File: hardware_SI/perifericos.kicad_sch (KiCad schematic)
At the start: 8 parts

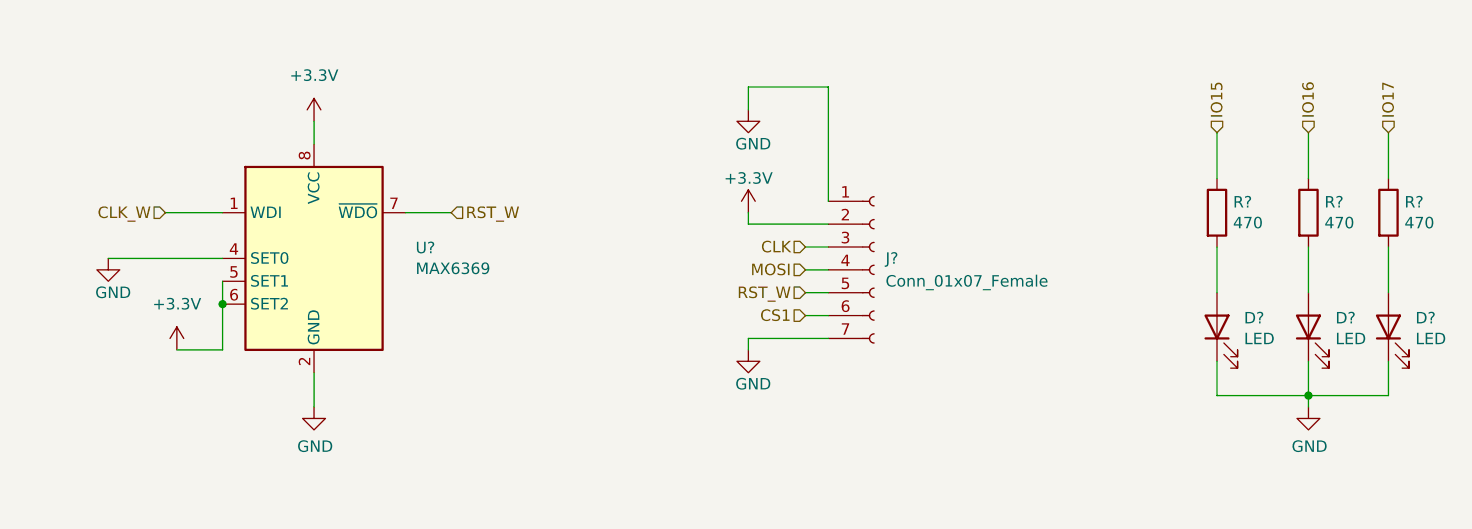
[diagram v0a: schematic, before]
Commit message: Etq compon, C desacop, ferrita
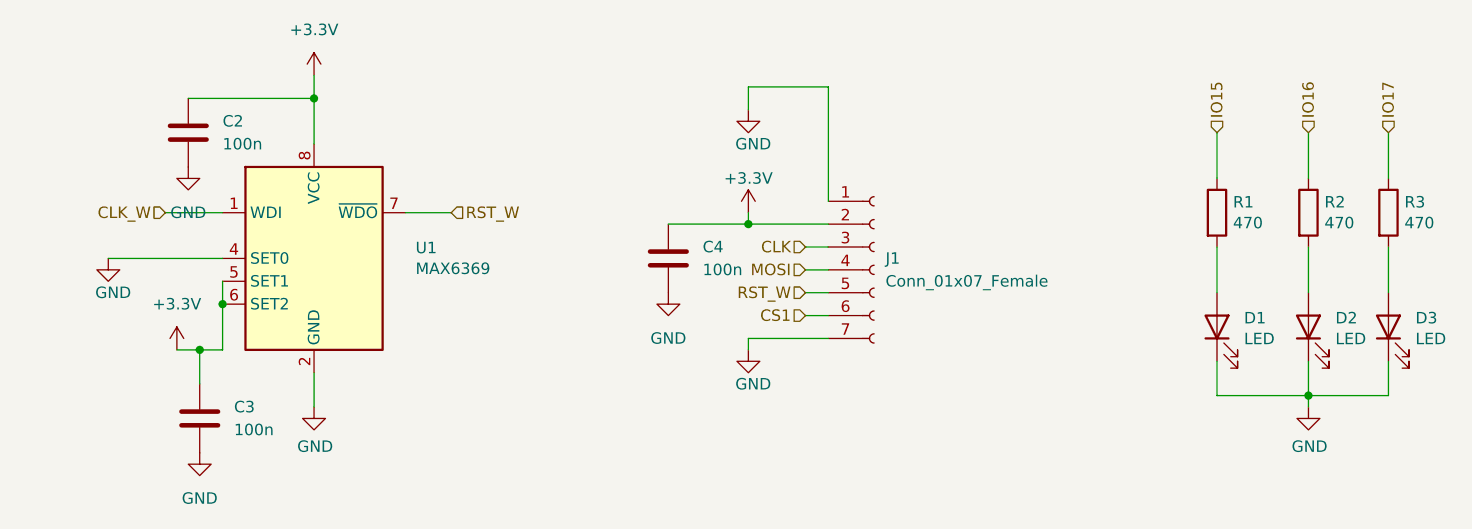
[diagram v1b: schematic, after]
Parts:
- added C2, C3, C4: 100n, symbol Device:C
- gave numbers to parts that had none: 8
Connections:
- net +3V3: now also C2.1, C3.1, C4.1
- net GND: now also C2.2, C3.2, C4.2
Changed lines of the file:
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@@
 (kicad_sch (version 20211123) (generator eeschema)
   (paper "A4")
+  (junction (at 93.98 76.2) (diameter 0) (color 0 0 0 0)
+  )
+  (junction (at 81.28 104.14) (diameter 0) (color 0 0 0 0)
+  )
   (junction (at 83.82 99.06) (diameter 0) (color 0 0 0 0)
   )
   (junction (at 204.47 109.22) (diameter 0) (color 0 0 0 0)
   )
+  (junction (at 142.24 90.17) (diameter 0) (color 0 0 0 0)
+  )
   (wire (pts (xy 151.13 90.17) (xy 142.24 90.17))
     (stroke (width 0) (type default) (color 0 0 0 0))
@@
     (stroke (width 0) (type default) (color 0 0 0 0))
   )
+  (wire (pts (xy 133.35 90.17) (xy 142.24 90.17))
+    (stroke (width 0) (type default) (color 0 0 0 0))
+  )
   (wire (pts (xy 151.13 102.87) (xy 142.24 102.87))
     (stroke (width 0) (type default) (color 0 0 0 0))
@@
     (stroke (width 0) (type default) (color 0 0 0 0))
   )
+  (wire (pts (xy 81.28 104.14) (xy 81.28 107.95))
+    (stroke (width 0) (type default) (color 0 0 0 0))
+  )
+  (wire (pts (xy 80.01 76.2) (xy 93.98 76.2))
+    (stroke (width 0) (type default) (color 0 0 0 0))
+  )
   (wire (pts (xy 213.36 85.09) (xy 213.36 80.01))
     (stroke (width 0) (type default) (color 0 0 0 0))
@@
     (stroke (width 0) (type default) (color 0 0 0 0))
   )
-  (wire (pts (xy 78.74 104.14) (xy 83.82 104.14))
+  (wire (pts (xy 78.74 104.14) (xy 81.28 104.14))
     (stroke (width 0) (type default) (color 0 0 0 0))
   )
@@
     (stroke (width 0) (type default) (color 0 0 0 0))
   )
+  (wire (pts (xy 93.98 76.2) (xy 93.98 81.28))
+    (stroke (width 0) (type default) (color 0 0 0 0))
+  )
   (wire (pts (xy 83.82 96.52) (xy 83.82 99.06))
     (stroke (width 0) (type default) (color 0 0 0 0))
@@
     (stroke (width 0) (type default) (color 0 0 0 0))
   )
+  (wire (pts (xy 81.28 104.14) (xy 83.82 104.14))
+    (stroke (width 0) (type default) (color 0 0 0 0))
+  )
   (wire (pts (xy 142.24 102.87) (xy 142.24 104.14))
     (stroke (width 0) (type default) (color 0 0 0 0))
   )
-  (wire (pts (xy 93.98 78.74) (xy 93.98 81.28))
+  (wire (pts (xy 93.98 73.66) (xy 93.98 76.2))
     (stroke (width 0) (type default) (color 0 0 0 0))
   )
@@
     (effects (font (size 1.27 1.27)) (justify left))
   )
+  (symbol (lib_id "Device:C") (at 133.35 93.98 0) (unit 1)
+    (in_bom yes) (on_board yes) (fields_autoplaced)
+    (property "Reference" "C4" (id 0) (at 137.16 92.7099 0)
+      (effects (font (size 1.27 1.27)) (justify left))
+    )
+    (property "Value" "100n" (id 1) (at 137.16 95.2499 0)
+      (effects (font (size 1.27 1.27)) (justify left))
+    )
+    (property "Footprint" "" (id 2) (at 134.3152 97.79 0)
+      (effects (font (size 1.27 1.27)) hide)
+    )
+    (property "Datasheet" "~" (id 3) (at 133.35 93.98 0)
+      (effects (font (size 1.27 1.27)) hide)
+    )
+    (pin "1")
+    (pin "2")
+  )
   (symbol (lib_id "power:GND") (at 71.12 93.98 0) (unit 1)
     (in_bom yes) (on_board yes)
@@
   (symbol (lib_id "Device:LED") (at 213.36 101.6 90) (unit 1)
     (in_bom yes) (on_board yes)
-    (property "Reference" "D?" (id 0) (at 216.3572 100.6094 90)
+    (property "Reference" "D3" (id 0) (at 216.3572 100.6094 90)
       (effects (font (size 1.27 1.27)) (justify right))
     )
@@
   (symbol (lib_id "Power_Supervisor:MAX6369") (at 93.98 93.98 0) (unit 1)
     (in_bom yes) (on_board yes)
-    (property "Reference" "U?" (id 0) (at 105.2576 92.8116 0)
+    (property "Reference" "U1" (id 0) (at 105.2576 92.8116 0)
       (effects (font (size 1.27 1.27)) (justify left))
     )
@@
   (symbol (lib_id "Device:R") (at 204.47 88.9 0) (unit 1)
     (in_bom yes) (on_board yes)
-    (property "Reference" "R?" (id 0) (at 206.248 87.7316 0)
+    (property "Reference" "R2" (id 0) (at 206.248 87.7316 0)
       (effects (font (size 1.27 1.27)) (justify left))
     )
@@
     (pin "2")
   )
+  (symbol (lib_id "Device:C") (at 81.28 111.76 0) (unit 1)
+    (in_bom yes) (on_board yes) (fields_autoplaced)
+    (property "Reference" "C3" (id 0) (at 85.09 110.4899 0)
+      (effects (font (size 1.27 1.27)) (justify left))
+    )
+    (property "Value" "100n" (id 1) (at 85.09 113.0299 0)
+      (effects (font (size 1.27 1.27)) (justify left))
+    )
+    (property "Footprint" "" (id 2) (at 82.2452 115.57 0)
+      (effects (font (size 1.27 1.27)) hide)
+    )
+    (property "Datasheet" "~" (id 3) (at 81.28 111.76 0)
+      (effects (font (size 1.27 1.27)) hide)
+    )
+    (pin "1")
+    (pin "2")
+  )
+  (symbol (lib_id "power:GND") (at 133.35 97.79 0) (unit 1)
+    (in_bom yes) (on_board yes) (fields_autoplaced)
+    (property "Reference" "#PWR?" (id 0) (at 133.35 104.14 0)
+      (effects (font (size 1.27 1.27)) hide)
+    )
+    (property "Value" "GND" (id 1) (at 133.35 102.87 0))
+    (property "Footprint" "" (id 2) (at 133.35 97.79 0)
+      (effects (font (size 1.27 1.27)) hide)
+    )
+    (property "Datasheet" "" (id 3) (at 133.35 97.79 0)
+      (effects (font (size 1.27 1.27)) hide)
+    )
+    (pin "1")
+  )
   (symbol (lib_id "power:GND") (at 142.24 104.14 0) (unit 1)
     (in_bom yes) (on_board yes)
@@
   (symbol (lib_id "Device:R") (at 213.36 88.9 0) (unit 1)
     (in_bom yes) (on_board yes)
-    (property "Reference" "R?" (id 0) (at 215.138 87.7316 0)
+    (property "Reference" "R3" (id 0) (at 215.138 87.7316 0)
       (effects (font (size 1.27 1.27)) (justify left))
     )
@@
   (symbol (lib_id "Device:R") (at 194.31 88.9 0) (unit 1)
     (in_bom yes) (on_board yes)
-    (property "Reference" "R?" (id 0) (at 196.088 87.7316 0)
+    (property "Reference" "R1" (id 0) (at 196.088 87.7316 0)
       (effects (font (size 1.27 1.27)) (justify left))
     )
@@
     (pin "1")
   )
-  (symbol (lib_id "power:+3.3V") (at 93.98 78.74 0) (unit 1)
-    (in_bom yes) (on_board yes) (fields_autoplaced)
-    (property "Reference" "#PWR?" (id 0) (at 93.98 82.55 0)
-      (effects (font (size 1.27 1.27)) hide)
-    )
-    (property "Value" "+3.3V" (id 1) (at 93.98 73.66 0))
-    (property "Footprint" "" (id 2) (at 93.98 78.74 0)
-      (effects (font (size 1.27 1.27)) hide)
-    )
-    (property "Datasheet" "" (id 3) (at 93.98 78.74 0)
+  (symbol (lib_id "power:+3.3V") (at 93.98 73.66 0) (unit 1)
+    (in_bom yes) (on_board yes) (fields_autoplaced)
+    (property "Reference" "#PWR?" (id 0) (at 93.98 77.47 0)
+      (effects (font (size 1.27 1.27)) hide)
+    )
+    (property "Value" "+3.3V" (id 1) (at 93.98 68.58 0))
+    (property "Footprint" "" (id 2) (at 93.98 73.66 0)
+      (effects (font (size 1.27 1.27)) hide)
+    )
+    (property "Datasheet" "" (id 3) (at 93.98 73.66 0)
       (effects (font (size 1.27 1.27)) hide)
     )
@@
   (symbol (lib_id "Device:LED") (at 204.47 101.6 90) (unit 1)
     (in_bom yes) (on_board yes)
-    (property "Reference" "D?" (id 0) (at 207.4672 100.6094 90)
+    (property "Reference" "D2" (id 0) (at 207.4672 100.6094 90)
       (effects (font (size 1.27 1.27)) (justify right))
     )
@@
     (pin "1")
     (pin "2")
+  )
+  (symbol (lib_id "power:GND") (at 81.28 115.57 0) (unit 1)
+    (in_bom yes) (on_board yes) (fields_autoplaced)
+    (property "Reference" "#PWR?" (id 0) (at 81.28 121.92 0)
+      (effects (font (size 1.27 1.27)) hide)
+    )
+    (property "Value" "GND" (id 1) (at 81.28 120.65 0))
+    (property "Footprint" "" (id 2) (at 81.28 115.57 0)
+      (effects (font (size 1.27 1.27)) hide)
+    )
+    (property "Datasheet" "" (id 3) (at 81.28 115.57 0)
+      (effects (font (size 1.27 1.27)) hide)
+    )
+    (pin "1")
   )
   (symbol (lib_id "power:GND") (at 93.98 110.49 0) (unit 1)
@@
     (pin "1")
   )
+  (symbol (lib_id "power:GND") (at 80.01 83.82 0) (unit 1)
+    (in_bom yes) (on_board yes) (fields_autoplaced)
+    (property "Reference" "#PWR?" (id 0) (at 80.01 90.17 0)
+      (effects (font (size 1.27 1.27)) hide)
+    )
+    (property "Value" "GND" (id 1) (at 80.01 88.9 0))
+    (property "Footprint" "" (id 2) (at 80.01 83.82 0)
+      (effects (font (size 1.27 1.27)) hide)
+    )
+    (property "Datasheet" "" (id 3) (at 80.01 83.82 0)
+      (effects (font (size 1.27 1.27)) hide)
+    )
+    (pin "1")
+  )
   (symbol (lib_id "Device:LED") (at 194.31 101.6 90) (unit 1)
     (in_bom yes) (on_board yes)
-    (property "Reference" "D?" (id 0) (at 197.3072 100.6094 90)
+    (property "Reference" "D1" (id 0) (at 197.3072 100.6094 90)
       (effects (font (size 1.27 1.27)) (justify right))
     )
@@
   (symbol (lib_id "Connector:Conn_01x07_Female") (at 156.21 95.25 0) (unit 1)
     (in_bom yes) (on_board yes) (fields_autoplaced)
-    (property "Reference" "J?" (id 0) (at 157.48 93.9799 0)
+    (property "Reference" "J1" (id 0) (at 157.48 93.9799 0)
       (effects (font (size 1.27 1.27)) (justify left))
     )
@@
     (pin "7")
   )
+  (symbol (lib_id "Device:C") (at 80.01 80.01 0) (unit 1)
+    (in_bom yes) (on_board yes) (fields_autoplaced)
+    (property "Reference" "C2" (id 0) (at 83.82 78.7399 0)
+      (effects (font (size 1.27 1.27)) (justify left))
+    )
+    (property "Value" "100n" (id 1) (at 83.82 81.2799 0)
+      (effects (font (size 1.27 1.27)) (justify left))
+    )
+    (property "Footprint" "" (id 2) (at 80.9752 83.82 0)
+      (effects (font (size 1.27 1.27)) hide)
+    )
+    (property "Datasheet" "~" (id 3) (at 80.01 80.01 0)
+      (effects (font (size 1.27 1.27)) hide)
+    )
+    (pin "1")
+    (pin "2")
+  )
 )

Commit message: mod_WD, etiquetas y clocks
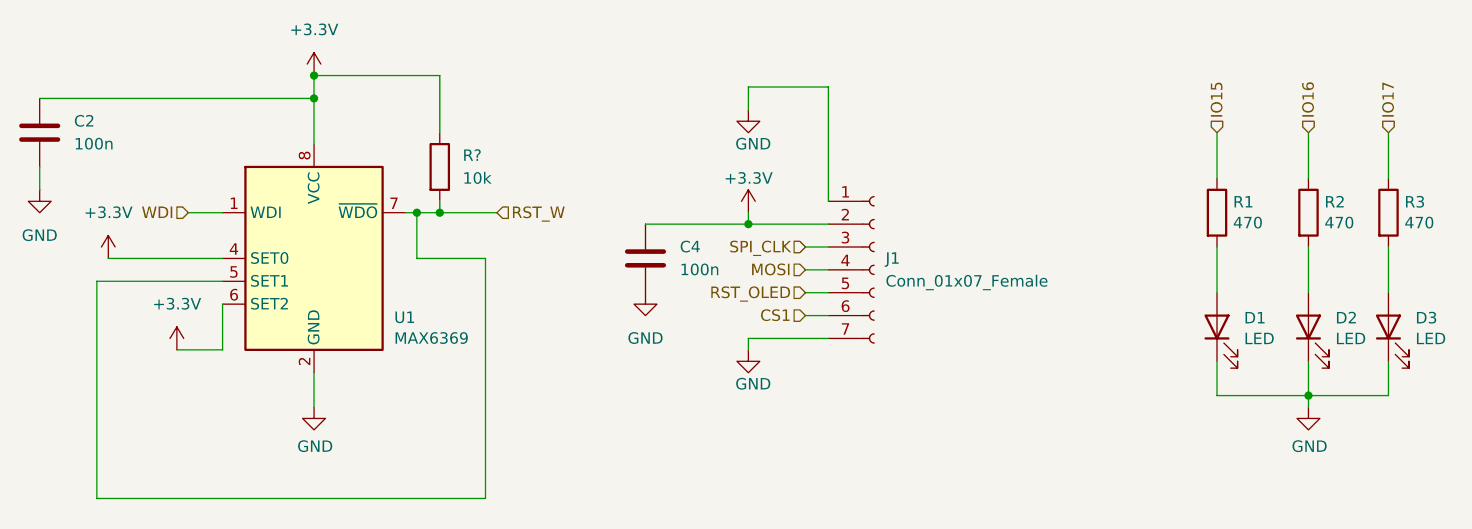
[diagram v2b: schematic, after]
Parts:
- removed C3: 100n, symbol Device:C
- added R?: 10k, Resistor_SMD:R_0805_2012Metric_Pad1.20x1.40mm_HandSolder, symbol Device:R
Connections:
- net +3V3: now also U1.4 (SET0), R?.1; no longer U1.5 (SET1)
- net GND: no longer U1.4 (SET0)
- net RST_W: now also U1.5 (SET1), R?.2; no longer J1.5 (Pin_5)
- net CLK renamed SPI_CLK
- net CLK_W renamed WDI
- new net RST_OLED: J1.5 (Pin_5)
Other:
- moved on the sheet: C2, C4

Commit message: USB Serial, huellas y correcciones ERC
- Se agregaron componentes para la comunicación serial con la Omega2+.
- Se actualizaron huellas en función de la disponibilidad de los componentes.
- Se ejecutó el ERC y se solucionaron los errores mostrados.
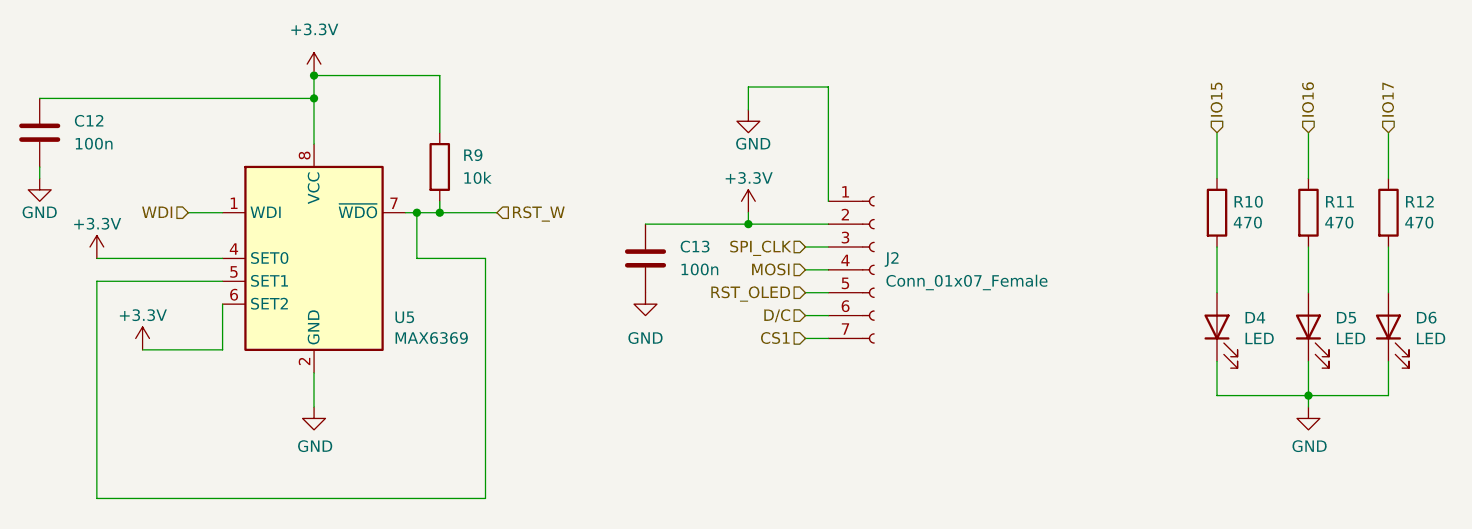
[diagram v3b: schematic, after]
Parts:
- gave numbers to parts that had none: 1
- renumbered C2 to C12, C4 to C13, D1 to D4, D2 to D5, D3 to D6, J1 to J2, R1 to R10, R2 to R11, R3 to R12, U1 to U5
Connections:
- net CS1: now also J2.7 (Pin_7); no longer J2.6 (Pin_6)
- net GND: no longer J2.7 (Pin_7)
- new net D/C: J2.6 (Pin_6)

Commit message: Definiciones PCB
- Se agregan definiciones para la creación de la PCB.
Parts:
- C12, C13: footprint (none) -> Capacitor_SMD:C_0805_2012Metric_Pad1.18x1.45mm_HandSolder
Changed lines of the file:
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@@
       (effects (font (size 1.27 1.27)) (justify left))
     )
-    (property "Footprint" "" (id 2) (at 131.7752 97.79 0)
+    (property "Footprint" "Capacitor_SMD:C_0805_2012Metric_Pad1.18x1.45mm_HandSolder" (id 2) (at 131.7752 97.79 0)
       (effects (font (size 1.27 1.27)) hide)
     )
@@
       (effects (font (size 1.27 1.27)) (justify left))
     )
-    (property "Footprint" "" (id 2) (at 64.4652 83.82 0)
-      (effects (font (size 1.27 1.27)) hide)
-    )
+    (property "Footprint" "Capacitor_SMD:C_0805_2012Metric_Pad1.18x1.45mm_HandSolder" (id 2) (at 64.4652 83.82 0)
+      (effects (font (size 1.27 1.27)) hide)
+    )
